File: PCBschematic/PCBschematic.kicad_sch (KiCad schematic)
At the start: 1 part, among them U1 STM32L412KBTx

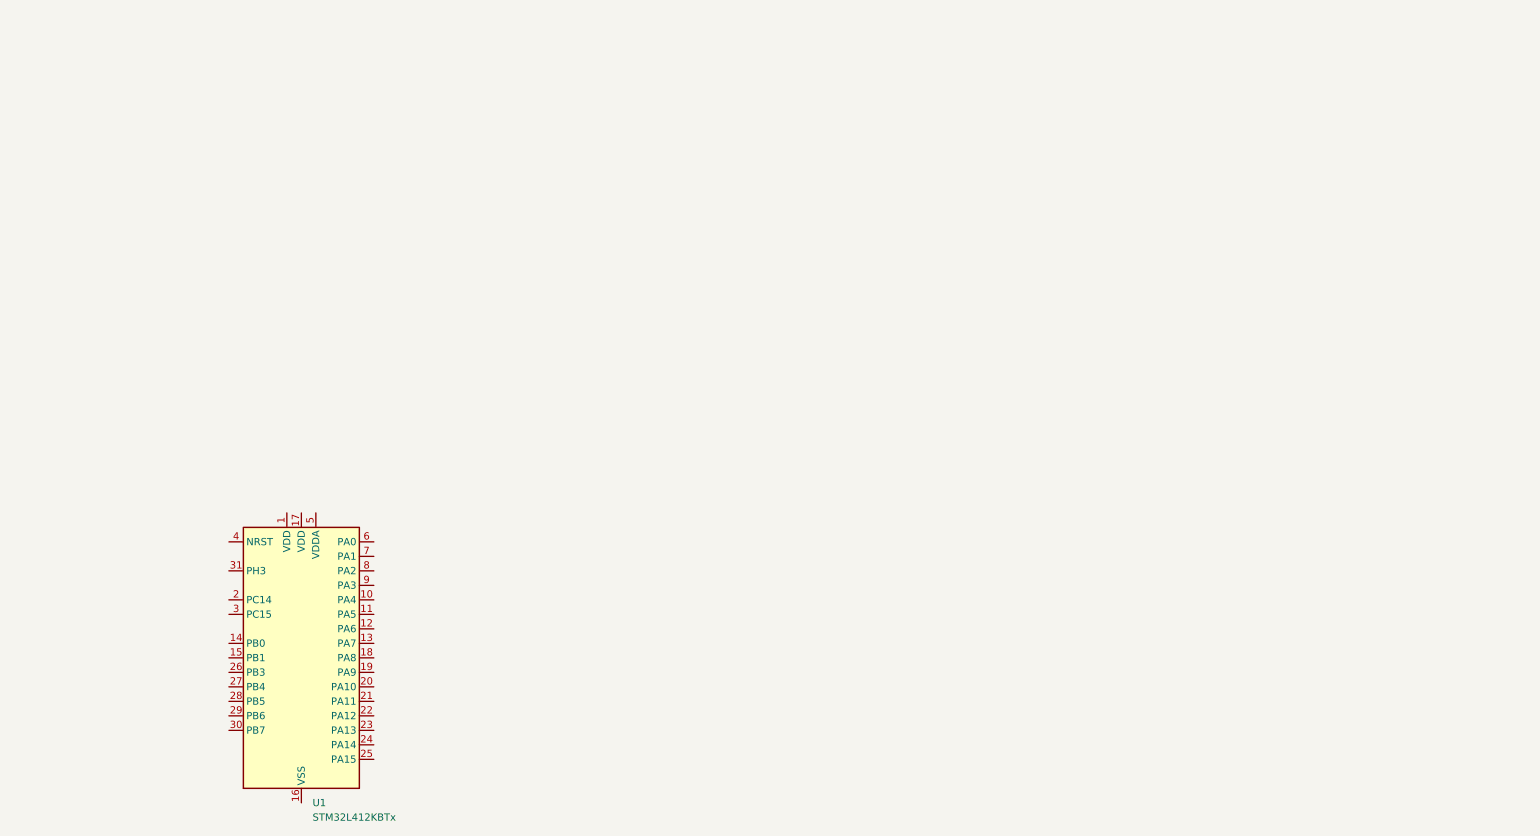
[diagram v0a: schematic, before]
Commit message: debutschematicpcb
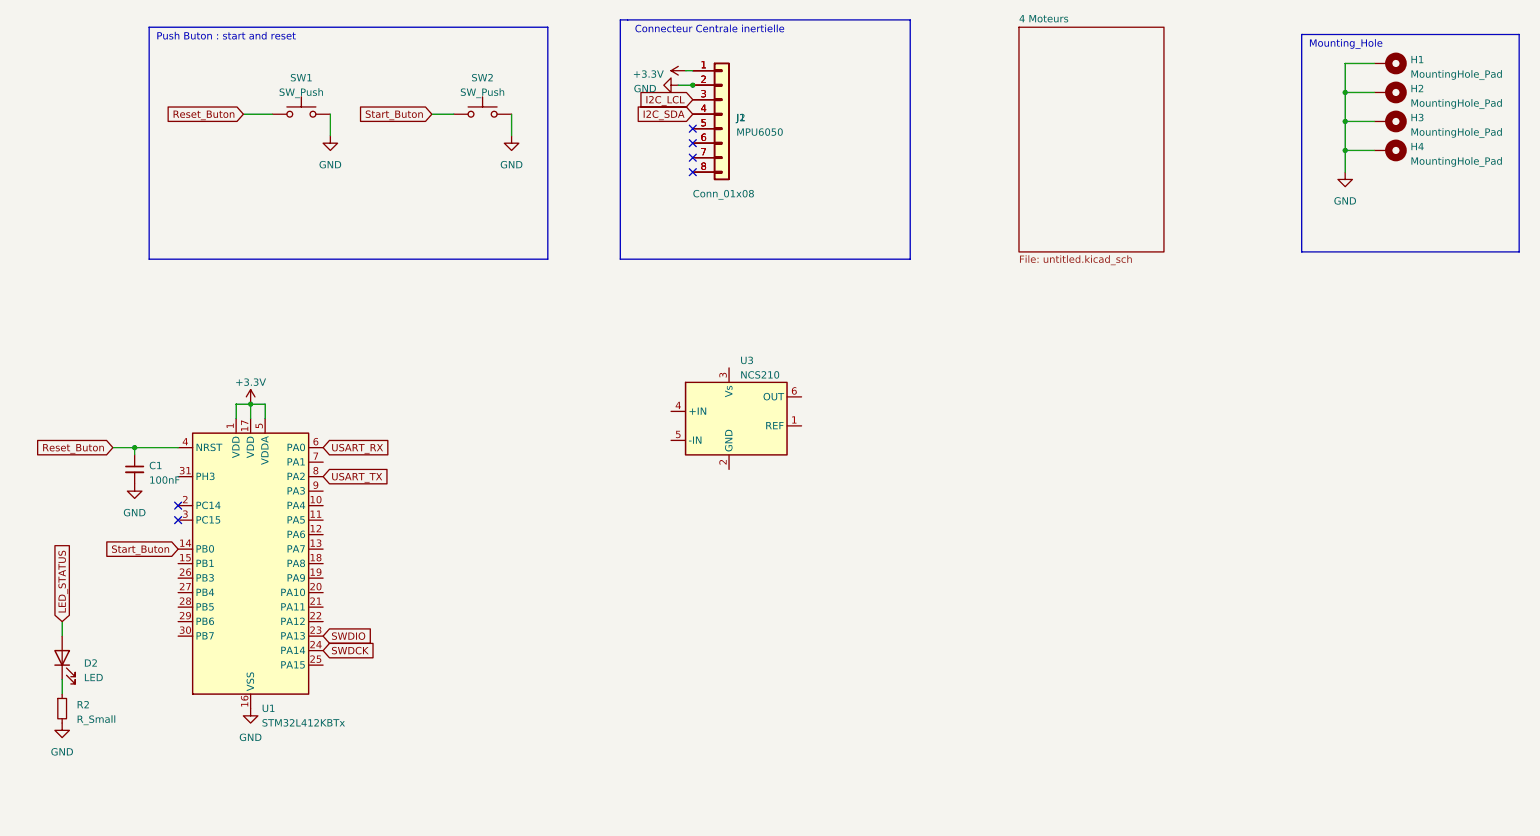
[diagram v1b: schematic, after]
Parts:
- added C1: 100nF, symbol Device:C_Small
- added D2: LED, symbol Device:LED
- added H1, H2, H3, H4: MountingHole_Pad, symbol Mechanical:MountingHole_Pad
- added J1: MPU6050, symbol Connector_Generic:Conn_01x08
- added J2: Conn_01x08, symbol Connector_Generic:Conn_01x08
- added R2: R_Small, symbol Device:R_Small
- added SW1, SW2: SW_Push, symbol Switch:SW_Push
- added U3: NCS210, Package_TO_SOT_SMD:SOT-363_SC-70-6, symbol Amplifier_Current:NCS210
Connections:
- net +3.3V: now reaches U1.1 (VDD)
- net +3.3V: now also U1.17 (VDD), U1.5 (VDDA), J1.1 (Pin_1), J2.1 (Pin_1)
- net Start_Buton: now reaches U1.14 (PB0)
- net Start_Buton: now also SW2.1
- net GND: now reaches U1.16 (VSS), U1.32 (VSS)
- net GND: now also C1.2, H1.1, H2.1, H3.1, H4.1, J1.2 (Pin_2), J2.2 (Pin_2), R2.2, SW1.2, SW2.2
- net SWDIO: now reaches U1.23 (PA13)
- net SWDCK: now reaches U1.24 (PA14)
- net Reset_Buton : now reaches U1.4 (NRST)
- net Reset_Buton : now also C1.1, SW1.1
- net USART_RX: now reaches U1.6 (PA0)
- net USART_TX: now reaches U1.8 (PA2)
- new net: J1.5 (Pin_5), J2.5 (Pin_5)
- new net: J1.6 (Pin_6), J2.6 (Pin_6)
- new net: J1.7 (Pin_7), J2.7 (Pin_7)
- new net: J1.8 (Pin_8), J2.8 (Pin_8)
- new net: D2.1 (K), R2.1
- new net I2C_LCL: J1.3 (Pin_3), J2.3 (Pin_3)
- new net I2C_SDA: J1.4 (Pin_4), J2.4 (Pin_4)
- new net LED_STATUS: D2.2 (A)
- no-connect marks 0 -> 6
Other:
- added sheet 4 Moteurs (untitled.kicad_sch)
- note added: "Connecteur Centrale inertielle"
- note added: "Mounting_Hole"
- note added: "Push Buton : start and reset"
- moved on the sheet: U1

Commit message: schematicavancee
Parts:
- removed U3: NCS210, Package_TO_SOT_SMD:SOT-363_SC-70-6, symbol Amplifier_Current:NCS210
- added C2: 4uF, symbol Device:C_Small
- added C3, C4: 100n, symbol Device:C_Small
- added C5, C6: C_Small, symbol Device:C_Small
- added J4: Conn_02x07_Odd_Even, symbol Connector_Generic:Conn_02x07_Odd_Even
- added L1: L_Small, symbol Device:L_Small
- added R4: 100, symbol Device:R_Small
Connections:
- net +3.3V: now also C2.1, C3.1, C4.1, J4.3 (Pin_3), L1.1
- net GND: now also C2.2, C3.2, C4.2, C5.2, C6.2, J4.11 (Pin_11), J4.5 (Pin_5), J4.7 (Pin_7), R4.2
- net LED_STATUS: now also U1.18 (PA8)
- net Reset_Buton : now also J4.12 (Pin_12)
- net SWDIO: now also J4.4 (Pin_4)
- net USART_RX: now also J4.13 (Pin_13)
- net USART_TX: now also J4.14 (Pin_14)
- net at U1.30 (PB7): now also R4.1
- new net +3.3VA: C5.1, C6.1, L1.2
- new net SWOCK: J4.6 (Pin_6)
- no-connect marks 6 -> 11
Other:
- note added: "SWD Connector"
- moved on the sheet: SW1, SW2

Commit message: newversion
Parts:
- added D3, D4: LED, symbol Device:LED
- added R3, R5: R_Small, symbol Device:R_Small
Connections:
- net GND: now also R3.2, R5.2
- new net: D3.1 (K), R3.1
- new net: D4.1 (K), R5.1
- new net LED_STM: D4.2 (A)
- new net LED_STOP: D3.2 (A)
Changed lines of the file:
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@@
+    (stroke (width 0) (type default))
+  )
+  (wire (pts (xy 107.95 129.54) (xy 107.95 132.08))
     (stroke (width 0) (type default))
   )
@@
     (stroke (width 0) (type default))
   )
+  (wire (pts (xy 95.25 129.54) (xy 95.25 132.08))
+    (stroke (width 0) (type default))
+  )
   (polyline (pts (xy 123.19 57.15) (xy 123.19 15.24))
     (stroke (width 0) (type default))
@@
     (stroke (width 0) (type default))
   )
+  (wire (pts (xy 95.25 119.38) (xy 95.25 121.92))
+    (stroke (width 0) (type default))
+  )
   (wire (pts (xy 74.93 33.02) (xy 78.74 33.02))
     (stroke (width 0) (type default))
@@
   )
   (wire (pts (xy 57.15 33.02) (xy 57.15 36.83))
+    (stroke (width 0) (type default))
+  )
+  (wire (pts (xy 107.95 119.38) (xy 107.95 121.92))
     (stroke (width 0) (type default))
   )
@@
     )
   )
+  (global_label "LED_STOP" (shape input) (at 95.25 119.38 90) (fields_autoplaced)
+    (effects (font (size 1.27 1.27)) (justify left))
+    (property "Intersheetrefs" "${INTERSHEET_REFS}" (at 95.25 107.2819 90)
+      (effects (font (size 1.27 1.27)) (justify left) hide)
+    )
+  )
   (global_label "Reset_Buton " (shape input) (at 34.29 90.17 180) (fields_autoplaced)
     (effects (font (size 1.27 1.27)) (justify right))
@@
     (effects (font (size 1.27 1.27)) (justify left))
     (property "Intersheetrefs" "${INTERSHEET_REFS}" (at 85.2138 110.49 0)
+      (effects (font (size 1.27 1.27)) (justify left) hide)
+    )
+  )
+  (global_label "LED_STM" (shape input) (at 107.95 119.38 90) (fields_autoplaced)
+    (effects (font (size 1.27 1.27)) (justify left))
+    (property "Intersheetrefs" "${INTERSHEET_REFS}" (at 107.95 108.431 90)
       (effects (font (size 1.27 1.27)) (justify left) hide)
     )
@@
     )
   )
+  (symbol (lib_id "Device:R_Small") (at 95.25 134.62 0) (unit 1)
+    (in_bom yes) (on_board yes) (dnp no) (fields_autoplaced)
+    (property "Reference" "R3" (at 97.79 133.985 0)
+      (effects (font (size 1.27 1.27)) (justify left))
+    )
+    (property "Value" "R_Small" (at 97.79 136.525 0)
+      (effects (font (size 1.27 1.27)) (justify left))
+    )
+    (property "Footprint" "" (at 95.25 134.62 0)
+      (effects (font (size 1.27 1.27)) hide)
+    )
+    (property "Datasheet" "~" (at 95.25 134.62 0)
+      (effects (font (size 1.27 1.27)) hide)
+    )
+    (pin "1")
+    (pin "2")
+    (instances
+      (project "PCBschematic"
+        (path "/cc300af8-7dc6-4303-a7a3-6c9320b23fa8"
+          (reference "R3") (unit 1)
+        )
+      )
+    )
+  )
   (symbol (lib_id "power:+3.3V") (at 158.75 111.76 0) (unit 1)
     (in_bom yes) (on_board yes) (dnp no) (fields_autoplaced)
@@
         (path "/cc300af8-7dc6-4303-a7a3-6c9320b23fa8"
           (reference "H4") (unit 1)
+        )
+      )
+    )
+  )
+  (symbol (lib_id "Device:R_Small") (at 107.95 134.62 0) (unit 1)
+    (in_bom yes) (on_board yes) (dnp no) (fields_autoplaced)
+    (property "Reference" "R5" (at 110.49 133.985 0)
+      (effects (font (size 1.27 1.27)) (justify left))
+    )
+    (property "Value" "R_Small" (at 110.49 136.525 0)
+      (effects (font (size 1.27 1.27)) (justify left))
+    )
+    (property "Footprint" "" (at 107.95 134.62 0)
+      (effects (font (size 1.27 1.27)) hide)
+    )
+    (property "Datasheet" "~" (at 107.95 134.62 0)
+      (effects (font (size 1.27 1.27)) hide)
+    )
+    (pin "1")
+    (pin "2")
+    (instances
+      (project "PCBschematic"
+        (path "/cc300af8-7dc6-4303-a7a3-6c9320b23fa8"
+          (reference "R5") (unit 1)
         )
       )
@@
     )
   )
+  (symbol (lib_id "power:GND") (at 95.25 137.16 0) (unit 1)
+    (in_bom yes) (on_board yes) (dnp no) (fields_autoplaced)
+    (property "Reference" "#PWR022" (at 95.25 143.51 0)
+      (effects (font (size 1.27 1.27)) hide)
+    )
+    (property "Value" "GND" (at 95.25 142.24 0)
+      (effects (font (size 1.27 1.27)))
+    )
+    (property "Footprint" "" (at 95.25 137.16 0)
+      (effects (font (size 1.27 1.27)) hide)
+    )
+    (property "Datasheet" "" (at 95.25 137.16 0)
+      (effects (font (size 1.27 1.27)) hide)
+    )
+    (pin "1")
+    (instances
+      (project "PCBschematic"
+        (path "/cc300af8-7dc6-4303-a7a3-6c9320b23fa8"
+          (reference "#PWR022") (unit 1)
+        )
+      )
+    )
+  )
   (symbol (lib_id "power:GND") (at 57.15 36.83 0) (unit 1)
     (in_bom yes) (on_board yes) (dnp no) (fields_autoplaced)
@@
     )
   )
+  (symbol (lib_id "Device:LED") (at 95.25 125.73 90) (unit 1)
+    (in_bom yes) (on_board yes) (dnp no) (fields_autoplaced)
+    (property "Reference" "D3" (at 99.06 126.6825 90)
+      (effects (font (size 1.27 1.27)) (justify right))
+    )
+    (property "Value" "LED" (at 99.06 129.2225 90)
+      (effects (font (size 1.27 1.27)) (justify right))
+    )
+    (property "Footprint" "" (at 95.25 125.73 0)
+      (effects (font (size 1.27 1.27)) hide)
+    )
+    (property "Datasheet" "~" (at 95.25 125.73 0)
+      (effects (font (size 1.27 1.27)) hide)
+    )
+    (pin "1")
+    (pin "2")
+    (instances
+      (project "PCBschematic"
+        (path "/cc300af8-7dc6-4303-a7a3-6c9320b23fa8"
+          (reference "D3") (unit 1)
+        )
+      )
+    )
+  )
+  (symbol (lib_id "Device:LED") (at 107.95 125.73 90) (unit 1)
+    (in_bom yes) (on_board yes) (dnp no) (fields_autoplaced)
+    (property "Reference" "D4" (at 111.76 126.6825 90)
+      (effects (font (size 1.27 1.27)) (justify right))
+    )
+    (property "Value" "LED" (at 111.76 129.2225 90)
+      (effects (font (size 1.27 1.27)) (justify right))
+    )
+    (property "Footprint" "" (at 107.95 125.73 0)
+      (effects (font (size 1.27 1.27)) hide)
+    )
+    (property "Datasheet" "~" (at 107.95 125.73 0)
+      (effects (font (size 1.27 1.27)) hide)
+    )
+    (pin "1")
+    (pin "2")
+    (instances
+      (project "PCBschematic"
+        (path "/cc300af8-7dc6-4303-a7a3-6c9320b23fa8"
+          (reference "D4") (unit 1)
+        )
+      )
+    )
+  )
   (symbol (lib_id "power:+3.3V") (at 134.62 24.13 90) (unit 1)
     (in_bom yes) (on_board yes) (dnp no) (fields_autoplaced)
@@
         )
       )
+    )
+  )
+  (symbol (lib_id "power:GND") (at 107.95 137.16 0) (unit 1)
+    (in_bom yes) (on_board yes) (dnp no) (fields_autoplaced)
+    (property "Reference" "#PWR023" (at 107.95 143.51 0)
+      (effects (font (size 1.27 1.27)) hide)
+    )
+    (property "Value" "GND" (at 107.95 142.24 0)
+      (effects (font (size 1.27 1.27)))
+    )
+    (property "Footprint" "" (at 107.95 137.16 0)
+      (effects (font (size 1.27 1.27)) hide)
+    )
+    (property "Datasheet" "" (at 107.95 137.16 0)
+      (effects (font (size 1.27 1.27)) hide)
+    )
+    (pin "1")
+    (instances
+      (project "PCBschematic"
+        (path "/cc300af8-7dc6-4303-a7a3-6c9320b23fa8"
+          (reference "#PWR023") (unit 1)
+        )
+      )

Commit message: stm32_pin_parametre
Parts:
- removed J1: MPU6050, symbol Connector_Generic:Conn_01x08
- removed J2: Conn_01x08, symbol Connector_Generic:Conn_01x08
- removed R4: 100, symbol Device:R_Small
- added C11: 200u, Capacitor_SMD:C_0603_1608Metric_Pad1.08x0.95mm_HandSolder, symbol Device:C_Small
- added J8: batterie_regulation_centraleinertielle, Connector_JST:JST_XH_B2B-XH-A_1x02_P2.50mm_Vertical, symbol Connector_Generic:Conn_01x02
- added J9: Conn_01x08, Connector_JST:JST_XH_B8B-XH-A_1x08_P2.50mm_Vertical, symbol Connector_Generic:Conn_01x08
- added U6: regulator_17395xx36, Package_TO_SOT_SMD:SOT-223-3_TabPin2, symbol Regulator_Linear:AMS1117-3.3
- C1, C3, C4: footprint (none) -> Capacitor_SMD:C_0603_1608Metric_Pad1.08x0.95mm_HandSolder
- C2: value 4uF -> 4.7uF; footprint (none) -> Capacitor_SMD:C_0603_1608Metric_Pad1.08x0.95mm_HandSolder
- C5: value C_Small -> 1u; footprint (none) -> Capacitor_SMD:C_0603_1608Metric_Pad1.08x0.95mm_HandSolder
- C6: value C_Small -> 10n; footprint (none) -> Capacitor_SMD:C_0603_1608Metric_Pad1.08x0.95mm_HandSolder
- D2, D3, D4: footprint (none) -> LED_SMD:LED_0603_1608Metric_Pad1.05x0.95mm_HandSolder
- H1, H2, H3, H4: footprint (none) -> MountingHole:MountingHole_3.2mm_M3_DIN965_Pad
- J4: footprint (none) -> Connector_Molex:Molex_Micro-Fit_3.0_43045-1612_2x08_P3.00mm_Vertical
- L1: value L_Small -> 39n; footprint (none) -> Inductor_SMD:L_0805_2012Metric_Pad1.15x1.40mm_HandSolder
- R2, R3, R5: value R_Small -> 1k; footprint (none) -> Resistor_SMD:R_0603_1608Metric_Pad0.98x0.95mm_HandSolder
- SW1, SW2: footprint (none) -> Button_Switch_THT:SW_Push_1P2T_Vertical_E-Switch_800UDP8P1A1M6
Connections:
- net LED_STM is gone; now on net LED_Start: D4.2 (A)
- net SWOCK is gone; now on net SWDCK: J4.6 (Pin_6)
- net +3.3V: now also J9.1 (Pin_1), U6.2 (VO)
- net GND: now also C11.2, J8.2 (Pin_2), J9.2 (Pin_2), U6.1 (GND)
- net I2C_SDA: now also U1.30 (PB7), J9.4 (Pin_4)
- net LED_STATUS: now also U1.27 (PB4); no longer U1.18 (PA8)
- net LED_STOP: now also U1.26 (PB3)
- net PWM_2: now reaches U1.19 (PA9)
- net PWM_3: now reaches U1.20 (PA10)
- net PWM_4: now reaches U1.21 (PA11)
- net LED_Start: now reaches U1.25 (PA15)
- net I2C_SCL: now reaches U1.29 (PB6)
- net I2C_SCL: now also J9.3 (Pin_3)
- net USART2_RX: now reaches U1.9 (PA3)
- net USART2_RX: now also J4.13 (Pin_13)
- net USART_RX: no longer names the net of U1.6 (PA0)
- net USART_RX: no longer J4.13 (Pin_13)
- net USART_TX renamed USART2_TX
- new net +7.5V: C11.1, J8.1 (Pin_1), U6.3 (VI)
- new net PWM_1: U1.18 (PA8)
- no-connect marks 11 -> 16
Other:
- note added: "Regulator"
- note added: "STM32"
- moved on the sheet: J4

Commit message: pcb schematic sans erreur et editeur sans erreur egalement
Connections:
- net AO3: now reaches U1.10 (PA4)
- net AO4: now reaches U1.12 (PA6)
- net AO1: now reaches U1.6 (PA0)
- net AO2: now reaches U1.7 (PA1)
- no-connect marks 16 -> 17
